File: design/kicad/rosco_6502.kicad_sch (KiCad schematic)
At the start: 56 parts, among them IC1 W65C02SxP, IC2 ATF22V10C-7PX, IC3 XR68C681CJTR-F, IC4 NE555P, IC5 ATF22V10C-7PX, J1 UART_A, J2 UART_B, J3 Conn_01x06, J4 Conn_01x01_Male, J5 Conn_02x18_Odd_Even, J6 Conn_01x02_Male, J7 Jack-DC, Q1 3.6864MHz, U1 AS6C4008-55PCN, U2 AS6C62256-55PCN, U3 AT28C64B-15PU, U4 74HCT174, X1 14MHz

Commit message: Bank ROM
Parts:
- U3: value AT28C64B-15PU -> AT28C256-15PU; footprint Package_DIP:DIP-28_W15.24mm_Socket_LongPads -> Package_DIP:DIP-28_W15.24mm; symbol rosco_6502:AT28C64B -> rosco_6502:AT28C256
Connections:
- net D4: now also U4.14 (D5)
- net D5: now also U4.13 (D4)
- net GND: no longer U4.13 (D4), U4.14 (D5)
- net BANK5: now reaches U3.1 (A14)
- net BANK5: now also U4.12 (Q4)
- net BANK4: now reaches U3.26 (A13)
- net BANK4: now also U4.15 (Q5)
- no-connect marks 13 -> 11
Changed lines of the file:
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@@
   (title_block
     (title "rosco_6502")
-    (date "2022-07-16")
+    (date "2023-09-10")
     (rev "3")
     (company "The Really Old-School Company Limited")
-    (comment 1 "Copyright (c)2022 Ross Bamford & Contributors")
+    (comment 1 "Copyright (c)2022-2023 Ross Bamford & Contributors")
     (comment 2 "Open Source Hardware (CERN OHL)")
   )
@@
   (no_connect (at 106.68 125.095))
   (no_connect (at 106.68 122.555))
-  (no_connect (at 220.345 132.715))
-  (no_connect (at 220.345 135.255))
   (no_connect (at 166.37 142.875))
   (no_connect (at 166.37 147.955))
@@
     (effects (font (size 1.27 1.27)) (justify left bottom))
   )
+  (global_label "BANK5" (shape output) (at 220.345 132.715 0) (fields_autoplaced)
+    (effects (font (size 1.27 1.27)) (justify left))
+    (property "Intersheet References" "${INTERSHEET_REFS}" (id 0) (at 228.9267 132.6356 0)
+      (effects (font (size 1.27 1.27)) (justify left) hide)
+    )
+  )
   (global_label "VCC" (shape passive) (at 45.085 120.015 90) (fields_autoplaced)
     (effects (font (size 1.27 1.27)) (justify left))
@@
     )
   )
-  (global_label "GND" (shape passive) (at 194.945 135.255 180) (fields_autoplaced)
+  (global_label "D5" (shape input) (at 194.945 132.715 180) (fields_autoplaced)
     (effects (font (size 1.27 1.27)) (justify right))
-    (property "Intersheet References" "${INTERSHEET_REFS}" (id 0) (at 188.6614 135.1756 0)
+    (property "Intersheet References" "${INTERSHEET_REFS}" (id 0) (at 190.0524 132.6356 0)
       (effects (font (size 1.27 1.27)) (justify right) hide)
     )
@@
     )
   )
-  (global_label "GND" (shape passive) (at 194.945 132.715 180) (fields_autoplaced)
+  (global_label "D4" (shape input) (at 194.945 135.255 180) (fields_autoplaced)
     (effects (font (size 1.27 1.27)) (justify right))
-    (property "Intersheet References" "${INTERSHEET_REFS}" (id 0) (at 188.6614 132.6356 0)
+    (property "Intersheet References" "${INTERSHEET_REFS}" (id 0) (at 190.0524 135.1756 0)
       (effects (font (size 1.27 1.27)) (justify right) hide)
     )
@@
     )
   )
+  (global_label "BANK4" (shape output) (at 220.345 135.255 0) (fields_autoplaced)
+    (effects (font (size 1.27 1.27)) (justify left))
+    (property "Intersheet References" "${INTERSHEET_REFS}" (id 0) (at 228.9267 135.1756 0)
+      (effects (font (size 1.27 1.27)) (justify left) hide)
+    )
+  )
   (global_label "A5" (shape input) (at 256.54 74.93 180) (fields_autoplaced)
     (effects (font (size 1.27 1.27)) (justify right))
@@
     )
   )
+  (global_label "BANK4" (shape input) (at 182.245 60.325 180) (fields_autoplaced)
+    (effects (font (size 1.27 1.27)) (justify right))
+    (property "Intersheet References" "${INTERSHEET_REFS}" (id 0) (at 173.6633 60.2456 0)
+      (effects (font (size 1.27 1.27)) (justify right) hide)
+    )
+  )
   (global_label "A7" (shape input) (at 182.245 45.085 180) (fields_autoplaced)
     (effects (font (size 1.27 1.27)) (justify right))
@@
     )
   )
+  (global_label "BANK5" (shape input) (at 182.245 62.865 180) (fields_autoplaced)
+    (effects (font (size 1.27 1.27)) (justify right))
+    (property "Intersheet References" "${INTERSHEET_REFS}" (id 0) (at 173.6633 62.7856 0)
+      (effects (font (size 1.27 1.27)) (justify right) hide)
+    )
+  )
   (global_label "VCC" (shape passive) (at 176.53 114.935 90) (fields_autoplaced)
     (effects (font (size 1.27 1.27)) (justify left))
@@
     (pin "2")
   )
-  (symbol (lib_id "rosco_6502:AT28C64B") (at 194.945 50.165 0) (unit 1)
+  (symbol (lib_id "rosco_6502:AT28C256") (at 194.945 50.165 0) (unit 1)
     (in_bom yes) (on_board yes) (fields_autoplaced)
     (property "Reference" "U3" (id 0) (at 196.9644 19.685 0)
       (effects (font (size 1.27 1.27)) (justify left))
     )
-    (property "Value" "AT28C64B-15PU" (id 1) (at 196.9644 22.225 0)
+    (property "Value" "AT28C256-15PU" (id 1) (at 196.9644 22.225 0)
       (effects (font (size 1.27 1.27)) (justify left))
     )
-    (property "Footprint" "Package_DIP:DIP-28_W15.24mm_Socket_LongPads" (id 2) (at 194.945 92.075 0)
+    (property "Footprint" "Package_DIP:DIP-28_W15.24mm" (id 2) (at 194.945 92.075 0)
       (effects (font (size 1.27 1.27)) hide)
     )
-    (property "Datasheet" "https://ww1.microchip.com/downloads/aemDocuments/documents/MPD/ProductDocuments/DataSheets/AT28C64B-64K-%288Kx8%29-Industrial-Parallel-EEPROM-with-Page-Write-and-Software-Data-Protection-20006432A.pdf" (id 3) (at 194.945 89.535 0)
+    (property "Datasheet" "https://ww1.microchip.com/downloads/en/DeviceDoc/doc0006.pdf" (id 3) (at 194.945 89.535 0)
       (effects (font (size 1.27 1.27)) hide)
     )
@@
     )
     (path "/4538bf2d-4cfd-4cc4-8255-e988871e9c9f"
-      (reference "U3") (unit 1) (value "AT28C64B-15PU") (footprint "Package_DIP:DIP-28_W15.24mm_Socket_LongPads")
+      (reference "U3") (unit 1) (value "AT28C256-15PU") (footprint "Package_DIP:DIP-28_W15.24mm")
     )
     (path "/7935fa25-e96e-4855-a3e0-7a704a6c1626"

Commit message: Fix ROM footprint; README
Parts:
- U3: footprint Package_DIP:DIP-28_W15.24mm -> Package_DIP:DIP-28_W15.24mm_Socket_LongPads
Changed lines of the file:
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@@
       (effects (font (size 1.27 1.27)) (justify left))
     )
-    (property "Footprint" "Package_DIP:DIP-28_W15.24mm" (id 2) (at 194.945 92.075 0)
+    (property "Footprint" "Package_DIP:DIP-28_W15.24mm_Socket_LongPads" (id 2) (at 194.945 92.075 0)
       (effects (font (size 1.27 1.27)) hide)
     )
@@
     )
     (path "/4538bf2d-4cfd-4cc4-8255-e988871e9c9f"
-      (reference "U3") (unit 1) (value "AT28C256-15PU") (footprint "Package_DIP:DIP-28_W15.24mm")
+      (reference "U3") (unit 1) (value "AT28C256-15PU") (footprint "Package_DIP:DIP-28_W15.24mm_Socket_LongPads")
     )
     (path "/7935fa25-e96e-4855-a3e0-7a704a6c1626"

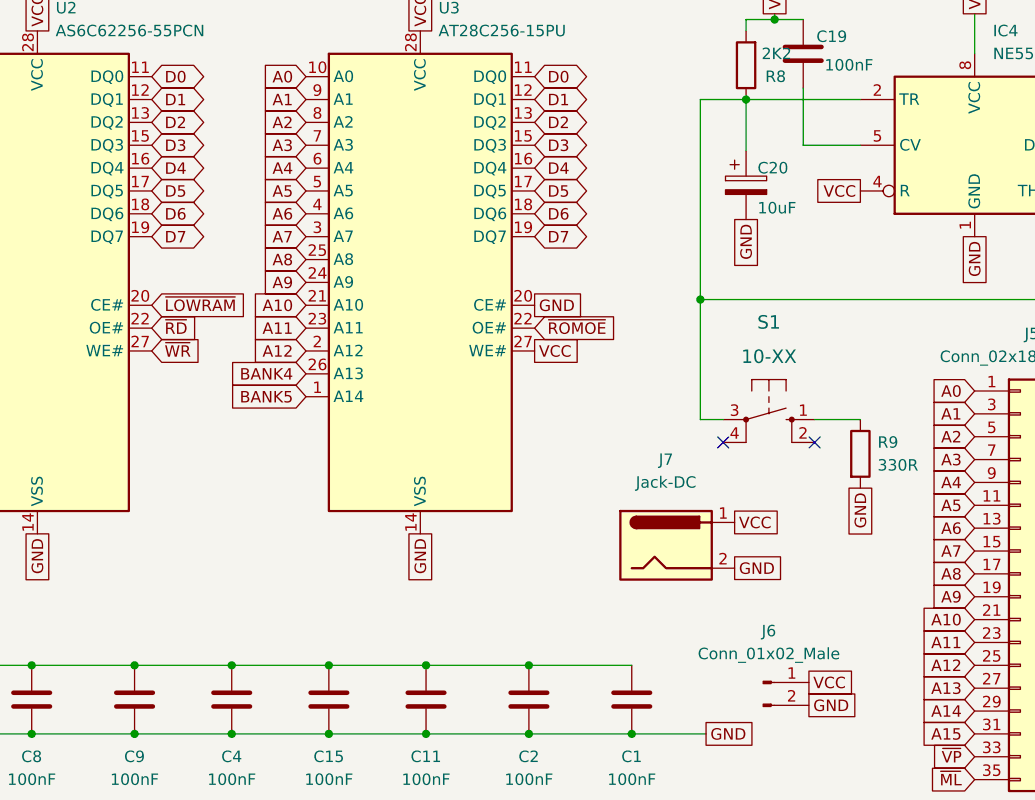
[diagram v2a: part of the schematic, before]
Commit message: Support other ROM as discussed https://discord.com/channels/698525682199822367/1004479727786012803/1005127547442429995
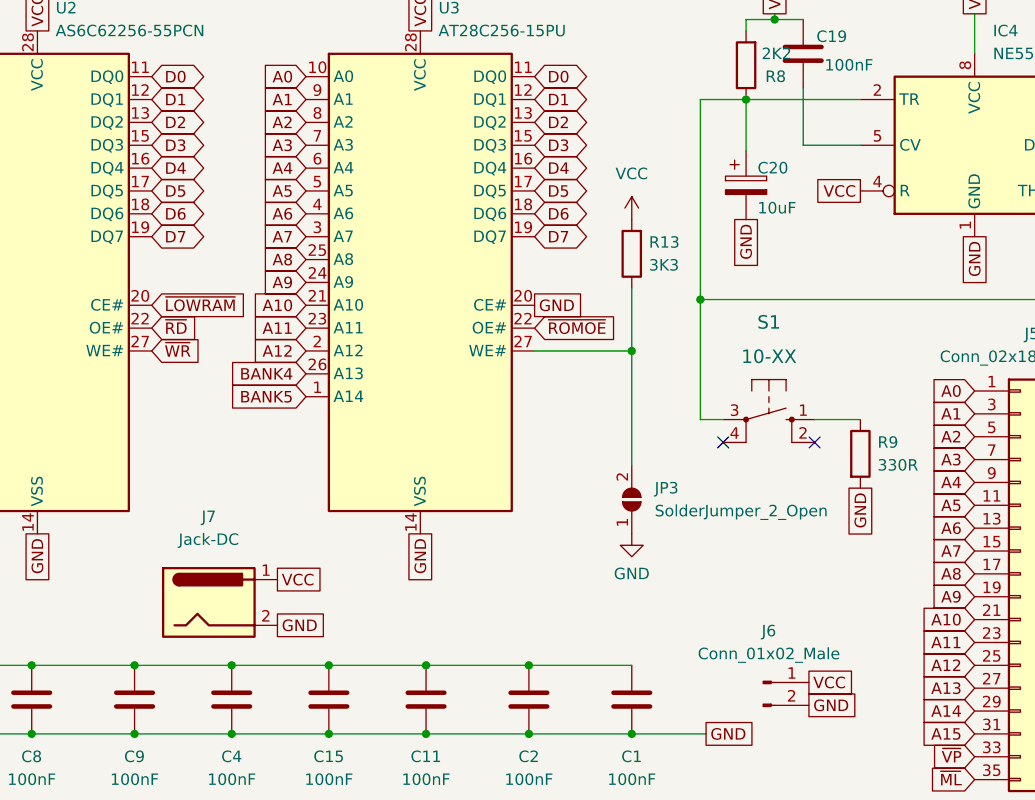
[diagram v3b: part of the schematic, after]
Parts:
- added JP3: SolderJumper_2_Open, Jumper:SolderJumper-2_P1.3mm_Open_TrianglePad1.0x1.5mm, symbol Jumper:SolderJumper_2_Open
- added R13: 3K3, Resistor_THT:R_Axial_DIN0207_L6.3mm_D2.5mm_P10.16mm_Horizontal, symbol Device:R
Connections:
- net GND: now also JP3.1 (A)
- net VCC: now also R13.2; no longer U3.27 (WE#)
- new net: JP3.2 (B), R13.1, U3.27 (WE#)
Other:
- moved on the sheet: J7
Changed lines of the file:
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@@
   (junction (at 27.305 132.715) (diameter 0) (color 0 0 0 0)
   )
+  (junction (at 218.44 57.785) (diameter 0) (color 0 0 0 0)
+  )
   (junction (at 27.305 99.695) (diameter 0) (color 0 0 0 0)
   )
@@
     (stroke (width 0) (type default) (color 0 0 0 0))
   )
+  (wire (pts (xy 207.645 57.785) (xy 218.44 57.785))
+    (stroke (width 0) (type default) (color 0 0 0 0))
+  )
   (wire (pts (xy 19.685 110.49) (xy 19.685 121.92))
     (stroke (width 0) (type default) (color 0 0 0 0))
@@
     (stroke (width 0) (type default) (color 0 0 0 0))
   )
+  (wire (pts (xy 218.44 57.785) (xy 218.44 70.485))
+    (stroke (width 0) (type default) (color 0 0 0 0))
+  )
   (wire (pts (xy 228.6 65.405) (xy 226.06 65.405))
     (stroke (width 0) (type default) (color 0 0 0 0))
@@
     (stroke (width 0) (type default) (color 0 0 0 0))
   )
+  (wire (pts (xy 218.44 57.785) (xy 218.44 50.8))
+    (stroke (width 0) (type default) (color 0 0 0 0))
+  )
   (wire (pts (xy 51.435 144.145) (xy 51.435 155.575))
     (stroke (width 0) (type default) (color 0 0 0 0))
@@
     )
   )
-  (global_label "VCC" (shape passive) (at 229.87 76.835 0) (fields_autoplaced)
+  (global_label "VCC" (shape passive) (at 179.07 83.185 0) (fields_autoplaced)
     (effects (font (size 1.27 1.27)) (justify left))
-    (property "Intersheet References" "${INTERSHEET_REFS}" (id 0) (at 235.9117 76.7556 0)
+    (property "Intersheet References" "${INTERSHEET_REFS}" (id 0) (at 185.1117 83.1056 0)
       (effects (font (size 1.27 1.27)) (justify left) hide)
     )
@@
     )
   )
-  (global_label "VCC" (shape passive) (at 207.645 57.785 0) (fields_autoplaced)
-    (effects (font (size 1.27 1.27)) (justify left))
-    (property "Intersheet References" "${INTERSHEET_REFS}" (id 0) (at 213.6867 57.7056 0)
-      (effects (font (size 1.27 1.27)) (justify left) hide)
-    )
-  )
   (global_label "A1" (shape input) (at 72.39 127.635 180) (fields_autoplaced)
     (effects (font (size 1.27 1.27)) (justify right))
@@
     )
   )
-  (global_label "GND" (shape passive) (at 229.87 81.915 0) (fields_autoplaced)
+  (global_label "GND" (shape passive) (at 179.07 88.265 0) (fields_autoplaced)
     (effects (font (size 1.27 1.27)) (justify left))
-    (property "Intersheet References" "${INTERSHEET_REFS}" (id 0) (at 236.1536 81.8356 0)
+    (property "Intersheet References" "${INTERSHEET_REFS}" (id 0) (at 185.3536 88.1856 0)
       (effects (font (size 1.27 1.27)) (justify left) hide)
     )
@@
     (pin "2")
   )
-  (symbol (lib_id "Connector:Jack-DC") (at 222.25 79.375 0) (unit 1)
+  (symbol (lib_id "Connector:Jack-DC") (at 171.45 85.725 0) (unit 1)
     (in_bom yes) (on_board yes) (fields_autoplaced)
-    (property "Reference" "J7" (id 0) (at 222.25 69.85 0))
-    (property "Value" "Jack-DC" (id 1) (at 222.25 72.39 0))
-    (property "Footprint" "Connector_BarrelJack:BarrelJack_Horizontal" (id 2) (at 223.52 80.391 0)
+    (property "Reference" "J7" (id 0) (at 171.45 76.2 0))
+    (property "Value" "Jack-DC" (id 1) (at 171.45 78.74 0))
+    (property "Footprint" "Connector_BarrelJack:BarrelJack_Horizontal" (id 2) (at 172.72 86.741 0)
       (effects (font (size 1.27 1.27)) hide)
     )
-    (property "Datasheet" "~" (id 3) (at 223.52 80.391 0)
+    (property "Datasheet" "~" (id 3) (at 172.72 86.741 0)
       (effects (font (size 1.27 1.27)) hide)
     )
@@
     (pin "2")
   )
+  (symbol (lib_id "Jumper:SolderJumper_2_Open") (at 218.44 74.295 90) (unit 1)
+    (in_bom yes) (on_board yes) (fields_autoplaced)
+    (property "Reference" "JP3" (id 0) (at 220.98 73.0249 90)
+      (effects (font (size 1.27 1.27)) (justify right))
+    )
+    (property "Value" "SolderJumper_2_Open" (id 1) (at 220.98 75.5649 90)
+      (effects (font (size 1.27 1.27)) (justify right))
+    )
+    (property "Footprint" "Jumper:SolderJumper-2_P1.3mm_Open_TrianglePad1.0x1.5mm" (id 2) (at 218.44 74.295 0)
+      (effects (font (size 1.27 1.27)) hide)
+    )
+    (property "Datasheet" "~" (id 3) (at 218.44 74.295 0)
+      (effects (font (size 1.27 1.27)) hide)
+    )
+    (pin "1")
+    (pin "2")
+  )
   (symbol (lib_id "Device:R") (at 34.29 41.275 0) (unit 1)
     (in_bom yes) (on_board yes) (fields_autoplaced)
@@
     (pin "2")
   )
+  (symbol (lib_id "power:GND") (at 218.44 78.105 0) (unit 1)
+    (in_bom yes) (on_board yes) (fields_autoplaced)
+    (property "Reference" "#PWR0102" (id 0) (at 218.44 84.455 0)
+      (effects (font (size 1.27 1.27)) hide)
+    )
+    (property "Value" "GND" (id 1) (at 218.44 82.55 0))
+    (property "Footprint" "" (id 2) (at 218.44 78.105 0)
+      (effects (font (size 1.27 1.27)) hide)
+    )
+    (property "Datasheet" "" (id 3) (at 218.44 78.105 0)
+      (effects (font (size 1.27 1.27)) hide)
+    )
+    (pin "1")
+  )
+  (symbol (lib_id "Device:R") (at 218.44 46.99 180) (unit 1)
+    (in_bom yes) (on_board yes) (fields_autoplaced)
+    (property "Reference" "R13" (id 0) (at 220.345 45.7199 0)
+      (effects (font (size 1.27 1.27)) (justify right))
+    )
+    (property "Value" "3K3" (id 1) (at 220.345 48.2599 0)
+      (effects (font (size 1.27 1.27)) (justify right))
+    )
+    (property "Footprint" "Resistor_THT:R_Axial_DIN0207_L6.3mm_D2.5mm_P10.16mm_Horizontal" (id 2) (at 220.218 46.99 90)
+      (effects (font (size 1.27 1.27)) hide)
+    )
+    (property "Datasheet" "~" (id 3) (at 218.44 46.99 0)
+      (effects (font (size 1.27 1.27)) hide)
+    )
+    (pin "1")
+    (pin "2")
+  )
   (symbol (lib_id "Device:R") (at 41.275 41.275 0) (unit 1)
     (in_bom yes) (on_board yes) (fields_autoplaced)
@@
     (pin "2")
   )
+  (symbol (lib_id "power:VCC") (at 218.44 43.18 0) (unit 1)
+    (in_bom yes) (on_board yes) (fields_autoplaced)
+    (property "Reference" "#PWR0101" (id 0) (at 218.44 46.99 0)
+      (effects (font (size 1.27 1.27)) hide)
+    )
+    (property "Value" "VCC" (id 1) (at 218.44 38.1 0))
+    (property "Footprint" "" (id 2) (at 218.44 43.18 0)
+      (effects (font (size 1.27 1.27)) hide)
+    )
+    (property "Datasheet" "" (id 3) (at 218.44 43.18 0)
+      (effects (font (size 1.27 1.27)) hide)
+    )
+    (pin "1")
+  )
   (symbol (lib_id "Device:C") (at 151.765 96.52 180) (unit 1)
     (in_bom yes) (on_board yes)
@@
       (reference "#FLG0101") (unit 1) (value "PWR_FLAG") (footprint "")
     )
+    (path "/ef632075-bd8e-431a-936e-ddcef8898460"
+      (reference "#PWR0101") (unit 1) (value "VCC") (footprint "")
+    )
+    (path "/5e8bdc10-ac5b-4b01-b3a4-291d79287e09"
+      (reference "#PWR0102") (unit 1) (value "GND") (footprint "")
+    )
     (path "/5e334318-0b3f-4566-a9f8-276ba232034c"
       (reference "C1") (unit 1) (value "100nF") (footprint "Capacitor_THT:C_Rect_L4.0mm_W2.5mm_P2.50mm")
@@
       (reference "JP2") (unit 1) (value "Jumper") (footprint "Connector_PinHeader_2.54mm:PinHeader_1x02_P2.54mm_Vertical")
     )
+    (path "/5b9a3805-90b0-44a6-a86e-5b6c07ff9037"
+      (reference "JP3") (unit 1) (value "SolderJumper_2_Open") (footprint "Jumper:SolderJumper-2_P1.3mm_Open_TrianglePad1.0x1.5mm")
+    )
     (path "/deb3ca0f-898f-4806-b894-f703676acdfc"
       (reference "LED1") (unit 1) (value "GREEN") (footprint "LED_THT:LED_D5.0mm")
@@
       (reference "R12") (unit 1) (value "3K3") (footprint "Resistor_THT:R_Axial_DIN0207_L6.3mm_D2.5mm_P10.16mm_Horizontal")
     )
+    (path "/671de7b2-5888-428d-91b7-46526dd6d8ef"
+      (reference "R13") (unit 1) (value "3K3") (footprint "Resistor_THT:R_Axial_DIN0207_L6.3mm_D2.5mm_P10.16mm_Horizontal")
+    )
     (path "/8a9d55c4-cad3-46c0-840f-2a6683619b87"

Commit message: Update for Kicad 7
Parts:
- IC4: footprint Package_DIP:DIP-8_W7.62mm_Socket_LongPads -> Package_DIP:DIP-8_W7.62mm
- J1, J2: symbol Connector:Conn_01x06_Male -> Connector:Conn_01x06_Pin
- J4: symbol Connector:Conn_01x01_Male -> Connector:Conn_01x01_Pin
- J6: value Conn_01x02_Male -> Conn_01x02_Pin; symbol Connector:Conn_01x02_Male -> Connector:Conn_01x02_Pin
